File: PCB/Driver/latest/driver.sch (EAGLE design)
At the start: 43 parts, among them IC1 STCS1PHR3D_AUTO, IC2 STCS1PHR3D_AUTO, IC3 STCS1PHR3D_AUTO, IC4 STCS1PHR3D_AUTO, IC5 STCS1PHR3D_AUTO, J1 1776275-2, J10 1776275-2, J17 1776275-2, J2 1776275-2, J3 1776275-2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

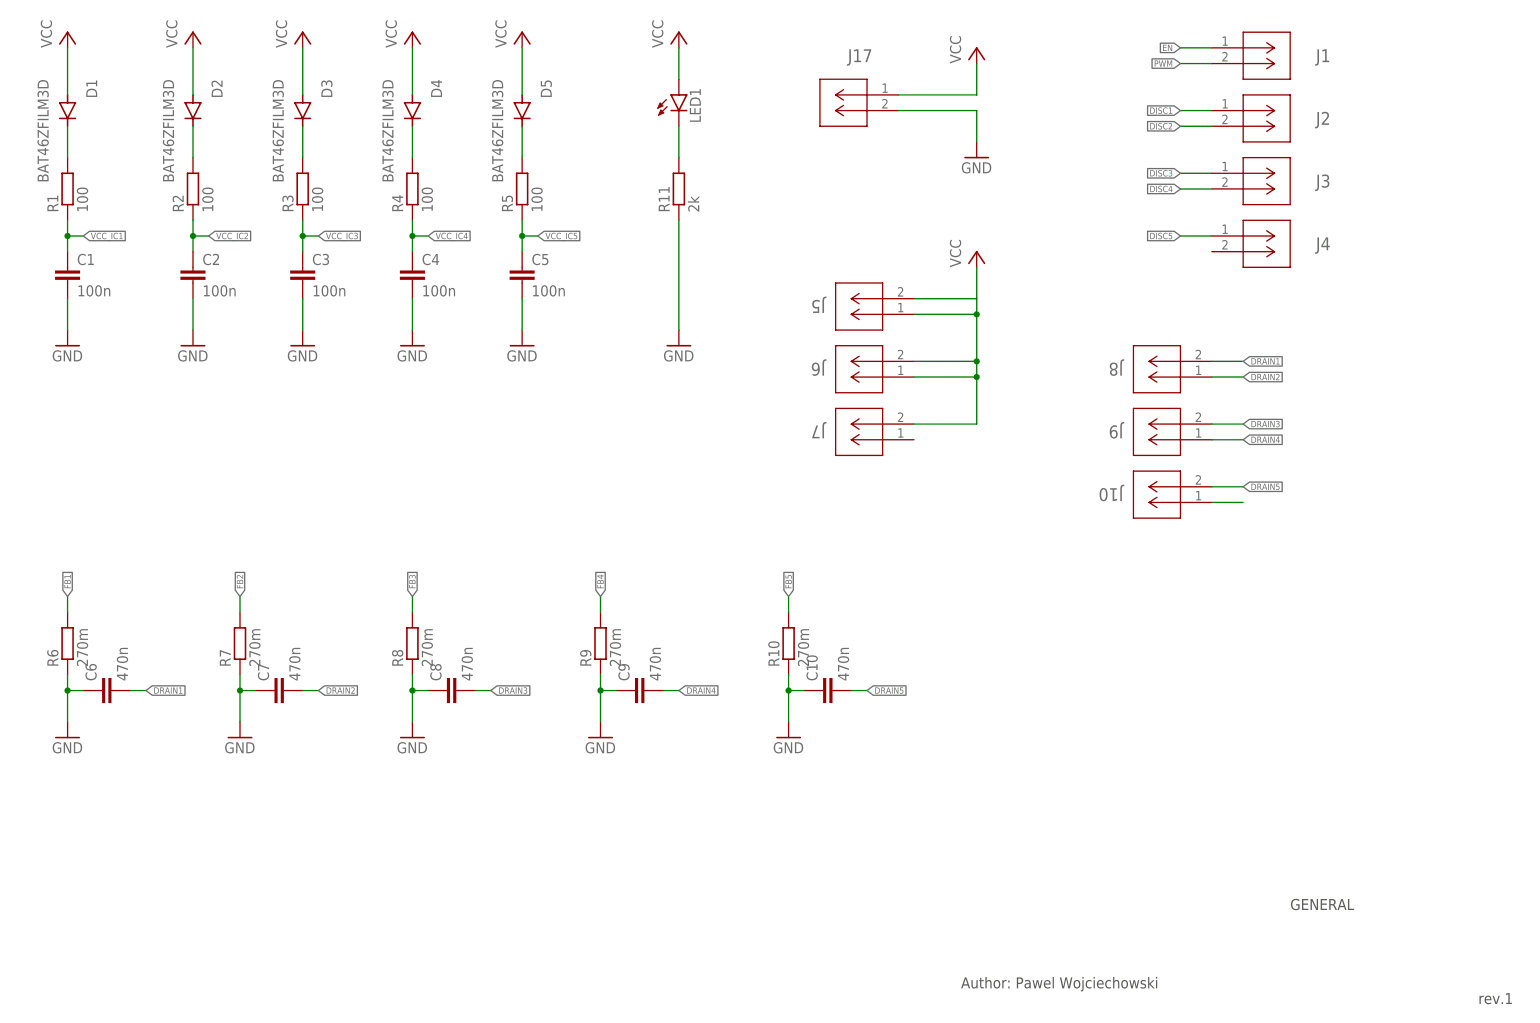
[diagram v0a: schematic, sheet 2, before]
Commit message: Driver LED
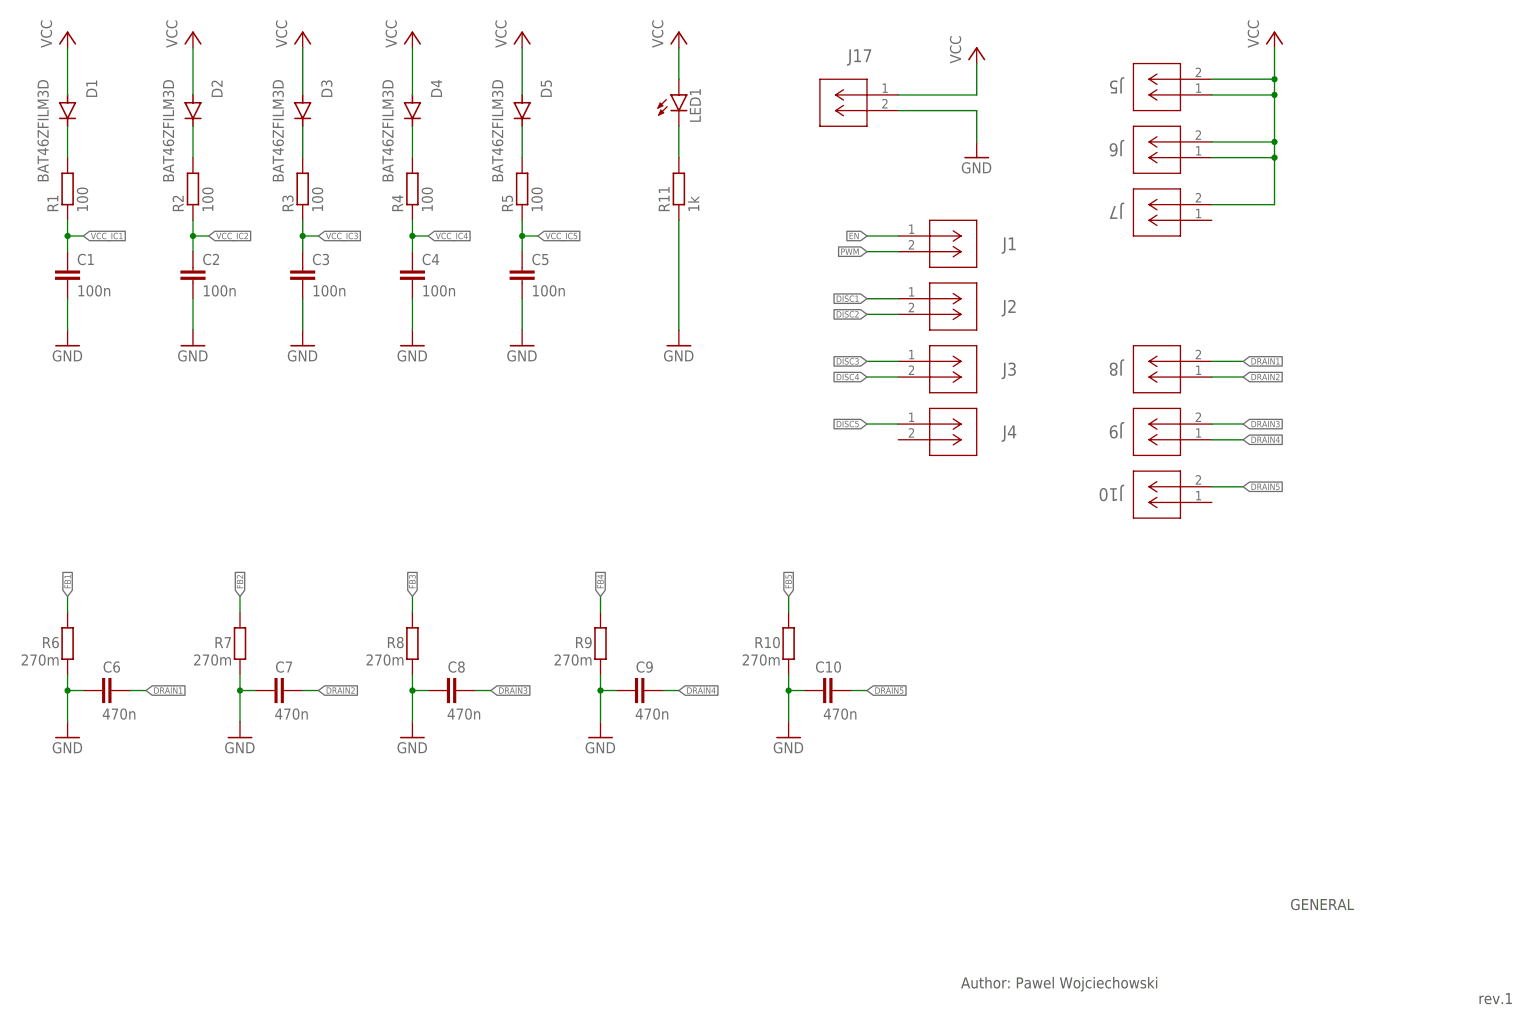
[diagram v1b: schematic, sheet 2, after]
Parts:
- R11: value 2k -> 1k
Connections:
- removed net N$16: J10.1
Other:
- moved on the sheet: J1, J2, J3, J4, J5, J6, J7
